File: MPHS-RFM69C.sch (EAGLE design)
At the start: 22 parts, among them U1 SPI_FLASH-X25XXSMD, U2 MCP1701

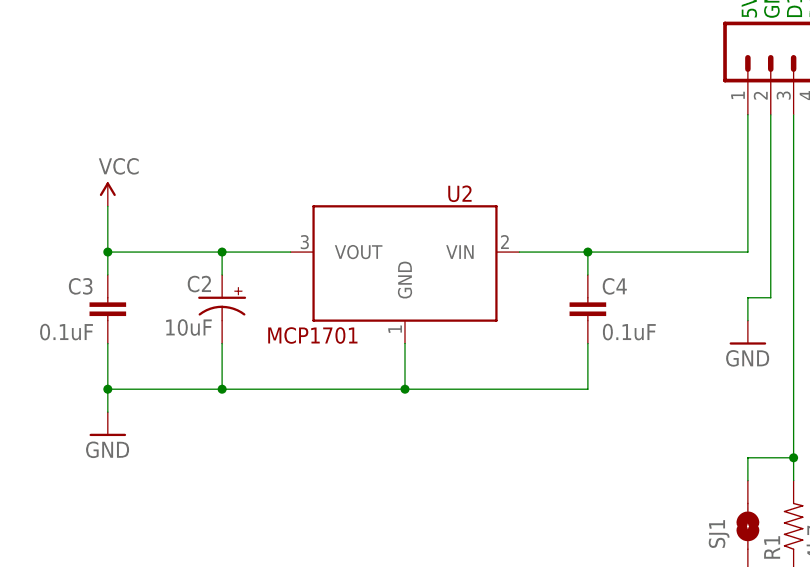
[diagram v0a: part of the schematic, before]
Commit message: Changed VReg to 1117
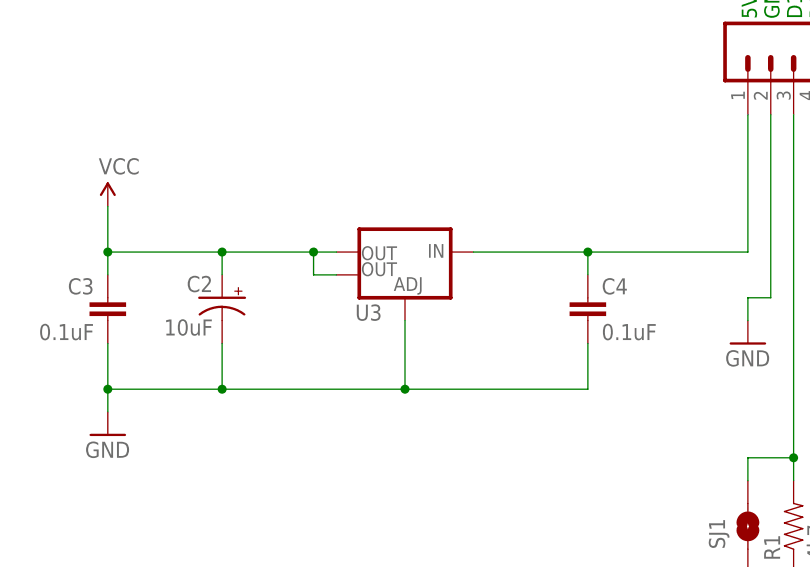
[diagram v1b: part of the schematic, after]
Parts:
- removed U2: MCP1701, ChipsParts:MCP1701
- added U3: (no value), SparkFun-PowerIC:V_REG_LM1117SOT223
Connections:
- net GND: now also U3.ADJ; no longer U2.GND
- net N$2: now also U3.IN; no longer U2.VIN
- net VCC: now also U3.OUT, U3.OUT@1; no longer U2.VOUT
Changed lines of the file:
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@@
 <layer number="56" name="wert" color="7" fill="1" visible="no" active="no"/>
 <layer number="57" name="tCAD" color="7" fill="1" visible="no" active="no"/>
+<layer number="59" name="tCarbon" color="7" fill="1" visible="no" active="no"/>
+<layer number="60" name="bCarbon" color="7" fill="1" visible="no" active="no"/>
 <layer number="90" name="Modules" color="5" fill="1" visible="yes" active="yes"/>
 <layer number="91" name="Nets" color="2" fill="1" visible="yes" active="yes"/>
@@
 <layer number="113" name="IDFDebug" color="4" fill="1" visible="yes" active="yes"/>
 <layer number="116" name="Patch_BOT" color="9" fill="4" visible="yes" active="yes"/>
+<layer number="118" name="Rect_Pads" color="7" fill="1" visible="no" active="yes"/>
 <layer number="121" name="_tsilk" color="7" fill="1" visible="yes" active="yes"/>
 <layer number="122" name="_bsilk" color="7" fill="1" visible="yes" active="yes"/>
@@
 <layer number="127" name="_tValues" color="7" fill="1" visible="yes" active="yes"/>
 <layer number="128" name="_bValues" color="7" fill="1" visible="yes" active="yes"/>
+<layer number="129" name="Mask" color="7" fill="1" visible="no" active="yes"/>
 <layer number="131" name="tAdjust" color="7" fill="1" visible="yes" active="yes"/>
 <layer number="132" name="bAdjust" color="7" fill="1" visible="yes" active="yes"/>
@@
 <layer number="223" name="223bmp" color="24" fill="1" visible="no" active="no"/>
 <layer number="224" name="224bmp" color="25" fill="1" visible="no" active="no"/>
+<layer number="225" name="225bmp" color="7" fill="1" visible="no" active="yes"/>
+<layer number="226" name="226bmp" color="7" fill="1" visible="no" active="yes"/>
+<layer number="227" name="227bmp" color="7" fill="1" visible="no" active="yes"/>
+<layer number="228" name="228bmp" color="7" fill="1" visible="no" active="yes"/>
+<layer number="229" name="229bmp" color="7" fill="1" visible="no" active="yes"/>
+<layer number="230" name="230bmp" color="7" fill="1" visible="no" active="yes"/>
+<layer number="231" name="231bmp" color="7" fill="1" visible="no" active="yes"/>
 <layer number="244" name="FP-Diffuser" color="14" fill="1" visible="yes" active="yes"/>
 <layer number="245" name="FP-Reveal" color="13" fill="1" visible="yes" active="yes"/>
@@
 <parts>
 <part name="FRAME1" library="SparkFun-Aesthetics" deviceset="FRAME-LETTER" device=""/>
-<part name="U2" library="ChipsParts" deviceset="MCP1701" device=""/>
 <part name="R1" library="SparkFun-Resistors" deviceset="RESISTOR" device="0805-RES" value="4k7"/>
 <part name="R2" library="SparkFun-Resistors" deviceset="RESISTOR" device="0805-RES" value="4k7"/>
@@
 <part name="SUPPLY6" library="SparkFun-Aesthetics" deviceset="VCC" device=""/>
 <part name="GND7" library="SparkFun-Aesthetics" deviceset="GND" device=""/>
+<part name="U3" library="SparkFun-PowerIC" deviceset="V_REG_LM1117" device="SOT223"/>
 </parts>
 <sheets>
@@
 <instance part="FRAME1" gate="G$1" x="-119.38" y="-101.6"/>
 <instance part="FRAME1" gate="G$2" x="27.94" y="-101.6"/>
-<instance part="U2" gate="G$1" x="-53.34" y="40.64" rot="MR0"/>
 <instance part="R1" gate="G$1" x="-10.16" y="12.7" rot="R90"/>
 <instance part="R2" gate="G$1" x="5.08" y="12.7" rot="R90"/>
@@
 <instance part="SUPPLY6" gate="1" x="63.5" y="-5.08"/>
 <instance part="GND7" gate="1" x="63.5" y="-35.56"/>
+<instance part="U3" gate="G$1" x="-53.34" y="43.18" rot="MR0"/>
 </instances>
 <busses>
@@
 <pinref part="C3" gate="G$1" pin="1"/>
 <wire x1="-86.36" y1="48.26" x2="-86.36" y2="43.18" width="0.1524" layer="91"/>
-<pinref part="U2" gate="G$1" pin="VOUT"/>
 <wire x1="-86.36" y1="43.18" x2="-86.36" y2="40.64" width="0.1524" layer="91"/>
-<wire x1="-66.04" y1="43.18" x2="-73.66" y2="43.18" width="0.1524" layer="91"/>
+<wire x1="-60.96" y1="43.18" x2="-63.5" y2="43.18" width="0.1524" layer="91"/>
 <pinref part="C2" gate="G$1" pin="+"/>
+<wire x1="-63.5" y1="43.18" x2="-73.66" y2="43.18" width="0.1524" layer="91"/>
 <wire x1="-73.66" y1="43.18" x2="-86.36" y2="43.18" width="0.1524" layer="91"/>
 <wire x1="-73.66" y1="40.64" x2="-73.66" y2="43.18" width="0.1524" layer="91"/>
 <junction x="-86.36" y="43.18"/>
 <junction x="-73.66" y="43.18"/>
+<pinref part="U3" gate="G$1" pin="OUT@1"/>
+<wire x1="-60.96" y1="40.64" x2="-63.5" y2="40.64" width="0.1524" layer="91"/>
+<wire x1="-63.5" y1="40.64" x2="-63.5" y2="43.18" width="0.1524" layer="91"/>
+<junction x="-63.5" y="43.18"/>
+<pinref part="U3" gate="G$1" pin="OUT"/>
 </segment>
 <segment>
@@
 <wire x1="-73.66" y1="27.94" x2="-86.36" y2="27.94" width="0.1524" layer="91"/>
 <wire x1="-73.66" y1="33.02" x2="-73.66" y2="27.94" width="0.1524" layer="91"/>
-<pinref part="U2" gate="G$1" pin="GND"/>
-<wire x1="-53.34" y1="33.02" x2="-53.34" y2="27.94" width="0.1524" layer="91"/>
+<wire x1="-53.34" y1="35.56" x2="-53.34" y2="27.94" width="0.1524" layer="91"/>
 <junction x="-53.34" y="27.94"/>
 <junction x="-73.66" y="27.94"/>
 <junction x="-86.36" y="27.94"/>
+<pinref part="U3" gate="G$1" pin="ADJ"/>
 </segment>
 <segment>
@@
 <net name="N$2" class="0">
 <segment>
-<pinref part="U2" gate="G$1" pin="VIN"/>
-<wire x1="-40.64" y1="43.18" x2="-33.02" y2="43.18" width="0.1524" layer="91"/>
+<wire x1="-45.72" y1="43.18" x2="-33.02" y2="43.18" width="0.1524" layer="91"/>
 <wire x1="-33.02" y1="43.18" x2="-15.24" y2="43.18" width="0.1524" layer="91"/>
 <wire x1="-15.24" y1="43.18" x2="-15.24" y2="58.42" width="0.1524" layer="91"/>
@@
 <junction x="-33.02" y="43.18"/>
 <pinref part="JP1" gate="G$1" pin="1"/>
+<pinref part="U3" gate="G$1" pin="IN"/>
 </segment>
 </net>
